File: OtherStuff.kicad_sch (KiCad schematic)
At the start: 35 parts, among them IC601 MMS9013-L-TP, IC602 MMS9013-L-TP, J601 USB_B_Micro, X601 XTAL_4_PINS, X602 XTAL_2_PINS

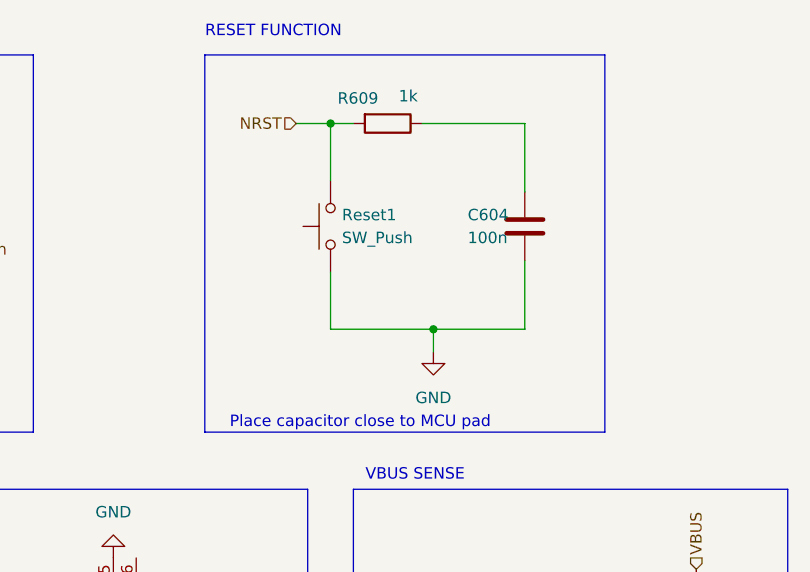
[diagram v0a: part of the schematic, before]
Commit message: Add FC0V104ZFTBR24 component library files
Added symbol, footprint, 3D model, and documentation files for the Supercap (FC0V104ZFTBR24) component across multiple EDA tool formats. Also updated schematic files and project backups, and removed obsolete autosave and backup files.
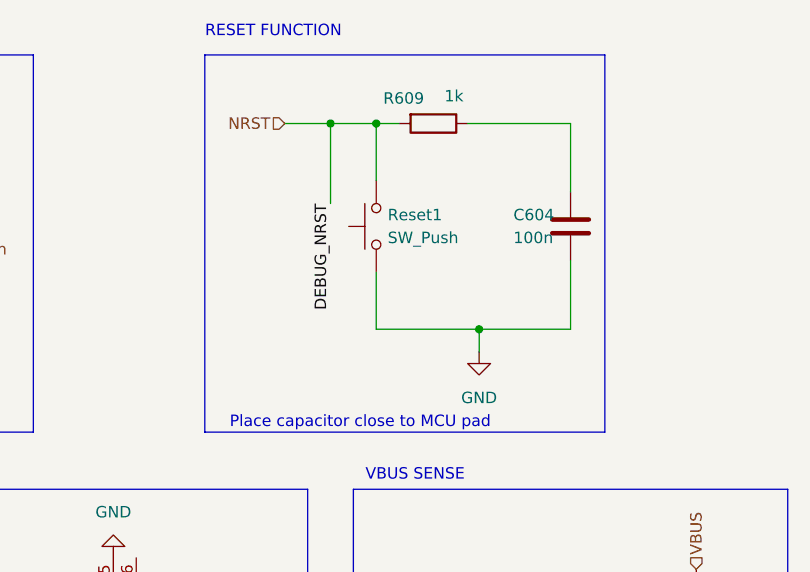
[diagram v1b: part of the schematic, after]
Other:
- moved on the sheet: C604, R609, Reset1
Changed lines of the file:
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@@
 	)
 	(junction
-		(at 97.79 29.21)
+		(at 102.87 29.21)
 		(diameter 0)
 		(color 0 0 0 0)
@@
 	)
 	(junction
+		(at 97.79 29.21)
+		(diameter 0)
+		(color 0 0 0 0)
+	)
+	(junction
 		(at 138.43 91.44)
 		(diameter 0)
@@
 	)
 	(junction
-		(at 109.22 52.07)
+		(at 114.3 52.07)
 		(diameter 0)
 		(color 0 0 0 0)
@@
 	(wire
 		(pts
-			(xy 119.38 36.83) (xy 119.38 29.21)
+			(xy 124.46 36.83) (xy 124.46 29.21)
 		)
 		(stroke
@@
 	(wire
 		(pts
-			(xy 109.22 52.07) (xy 97.79 52.07)
+			(xy 97.79 29.21) (xy 102.87 29.21)
+		)
+		(stroke
+			(width 0)
+			(type default)
+		)
+	)
+	(wire
+		(pts
+			(xy 114.3 52.07) (xy 102.87 52.07)
 		)
 		(stroke
@@
 	(wire
 		(pts
-			(xy 109.22 52.07) (xy 109.22 54.61)
+			(xy 114.3 52.07) (xy 114.3 54.61)
 		)
 		(stroke
@@
 	(wire
 		(pts
-			(xy 119.38 52.07) (xy 109.22 52.07)
+			(xy 124.46 52.07) (xy 114.3 52.07)
+		)
+		(stroke
+			(width 0)
+			(type default)
+		)
+	)
+	(wire
+		(pts
+			(xy 97.79 29.21) (xy 97.79 38.1)
 		)
 		(stroke
@@
 	(wire
 		(pts
-			(xy 97.79 52.07) (xy 97.79 45.72)
+			(xy 102.87 52.07) (xy 102.87 45.72)
 		)
 		(stroke
@@
 	(wire
 		(pts
-			(xy 97.79 29.21) (xy 100.33 29.21)
+			(xy 102.87 29.21) (xy 105.41 29.21)
 		)
 		(stroke
@@
 	(wire
 		(pts
-			(xy 93.98 29.21) (xy 97.79 29.21)
+			(xy 92.71 29.21) (xy 97.79 29.21)
 		)
 		(stroke
@@
 	(wire
 		(pts
-			(xy 119.38 29.21) (xy 107.95 29.21)
+			(xy 124.46 29.21) (xy 113.03 29.21)
 		)
 		(stroke
@@
 	(wire
 		(pts
-			(xy 119.38 44.45) (xy 119.38 52.07)
+			(xy 124.46 44.45) (xy 124.46 52.07)
 		)
 		(stroke
@@
 	(wire
 		(pts
-			(xy 97.79 35.56) (xy 97.79 29.21)
+			(xy 102.87 35.56) (xy 102.87 29.21)
 		)
 		(stroke
@@
 		)
 	)
+	(label "DEBUG_NRST"
+		(at 97.79 38.1 270)
+		(effects
+			(font
+				(size 1.27 1.27)
+			)
+			(justify right bottom)
+		)
+	)
 	(label "USB_1_D-"
 		(at 44.45 85.09 0)
@@
 	(hierarchical_label "NRST"
 		(shape input)
-		(at 93.98 29.21 180)
+		(at 92.71 29.21 180)
 		(effects
 			(font
@@
 	(symbol
 		(lib_id "Device:R")
-		(at 104.14 29.21 270)
+		(at 109.22 29.21 270)
 		(unit 1)
 		(exclude_from_sim no)
@@
 		(dnp no)
 		(property "Reference" "R609"
-			(at 100.838 26.416 90)
+			(at 105.918 26.416 90)
 			(effects
 				(font
@@
 		)
 		(property "Value" "1k"
-			(at 106.426 26.162 90)
+			(at 111.506 26.162 90)
 			(effects
 				(font
@@
 		)
 		(property "Footprint" "Resistor_SMD:R_0805_2012Metric_Pad1.20x1.40mm_HandSolder"
-			(at 104.14 27.432 90)
+			(at 109.22 27.432 90)
 			(effects
 				(font
@@
 		)
 		(property "Datasheet" "~"
-			(at 104.14 29.21 0)
+			(at 109.22 29.21 0)
 			(effects
 				(font
@@
 		)
 		(property "Description" ""
-			(at 104.14 29.21 0)
+			(at 109.22 29.21 0)
 			(effects
 				(font
@@
 		)
 		(property "Mouser Part Number" "279-CRG0805ZR"
-			(at 104.14 29.21 0)
+			(at 109.22 29.21 0)
 			(effects
 				(font
@@
 	(symbol
 		(lib_id "Device:C")
-		(at 119.38 40.64 180)
+		(at 124.46 40.64 180)
 		(unit 1)
 		(exclude_from_sim no)
@@
 		(dnp no)
 		(property "Reference" "C604"
-			(at 113.03 39.37 0)
+			(at 118.11 39.37 0)
 			(effects
 				(font
@@
 		)
 		(property "Value" "100n"
-			(at 113.03 41.91 0)
+			(at 118.11 41.91 0)
 			(effects
 				(font
@@
 		)
 		(property "Footprint" "Capacitor_SMD:C_0805_2012Metric_Pad1.18x1.45mm_HandSolder"
-			(at 118.4148 36.83 0)
+			(at 123.4948 36.83 0)
 			(effects
 				(font
@@
 		)
 		(property "Datasheet" "~"
-			(at 119.38 40.64 0)
+			(at 124.46 40.64 0)
 			(effects
 				(font
@@
 		)
 		(property "Description" ""
-			(at 119.38 40.64 0)
+			(at 124.46 40.64 0)
 			(effects
 				(font
@@
 		)
 		(property "Mouser Part Number" "187-CL21A226KQCLRNC"
-			(at 119.38 40.64 0)
+			(at 124.46 40.64 0)
 			(effects
 				(font
@@
 	(symbol
 		(lib_id "power:GND")
-		(at 109.22 54.61 0)
+		(at 114.3 54.61 0)
 		(unit 1)
 		(exclude_from_sim no)
@@
 		(fields_autoplaced yes)
 		(property "Reference" "#PWR0613"
-			(at 109.22 60.96 0)
+			(at 114.3 60.96 0)
 			(effects
 				(font
@@
 		)
 		(property "Value" "GND"
-			(at 109.22 59.69 0)
+			(at 114.3 59.69 0)
 			(effects
 				(font
@@
 		)
 		(property "Footprint" ""
-			(at 109.22 54.61 0)
+			(at 114.3 54.61 0)
 			(effects
 				(font
@@
 		)
 		(property "Datasheet" ""
-			(at 109.22 54.61 0)
+			(at 114.3 54.61 0)
 			(effects
 				(font
@@
 		)
 		(property "Description" "Power symbol creates a global label with name \"GND\" , ground"
-			(at 109.22 54.61 0)
+			(at 114.3 54.61 0)
 			(effects
 				(font
@@
 	(symbol
 		(lib_id "Switch:SW_Push")
-		(at 97.79 40.64 90)
+		(at 102.87 40.64 90)
 		(unit 1)
 		(exclude_from_sim no)
@@
 		(fields_autoplaced yes)
 		(property "Reference" "Reset1"
-			(at 99.06 39.3699 90)
+			(at 104.14 39.3699 90)
 			(effects
 				(font
@@
 		)
 		(property "Value" "SW_Push"
-			(at 99.06 41.9099 90)
+			(at 104.14 41.9099 90)
 			(effects
 				(font
@@
 		)
 		(property "Footprint" "Button_Switch_SMD:SW_Push_SPST_NO_Alps_SKRK"
-			(at 92.71 40.64 0)
+			(at 97.79 40.64 0)
 			(effects
 				(font
@@
 		)
 		(property "Datasheet" "~"
-			(at 92.71 40.64 0)
+			(at 97.79 40.64 0)
 			(effects
 				(font
@@
 		)
 		(property "Description" "Push button switch, generic, two pins"
-			(at 97.79 40.64 0)
+			(at 102.87 40.64 0)
 			(effects
 				(font

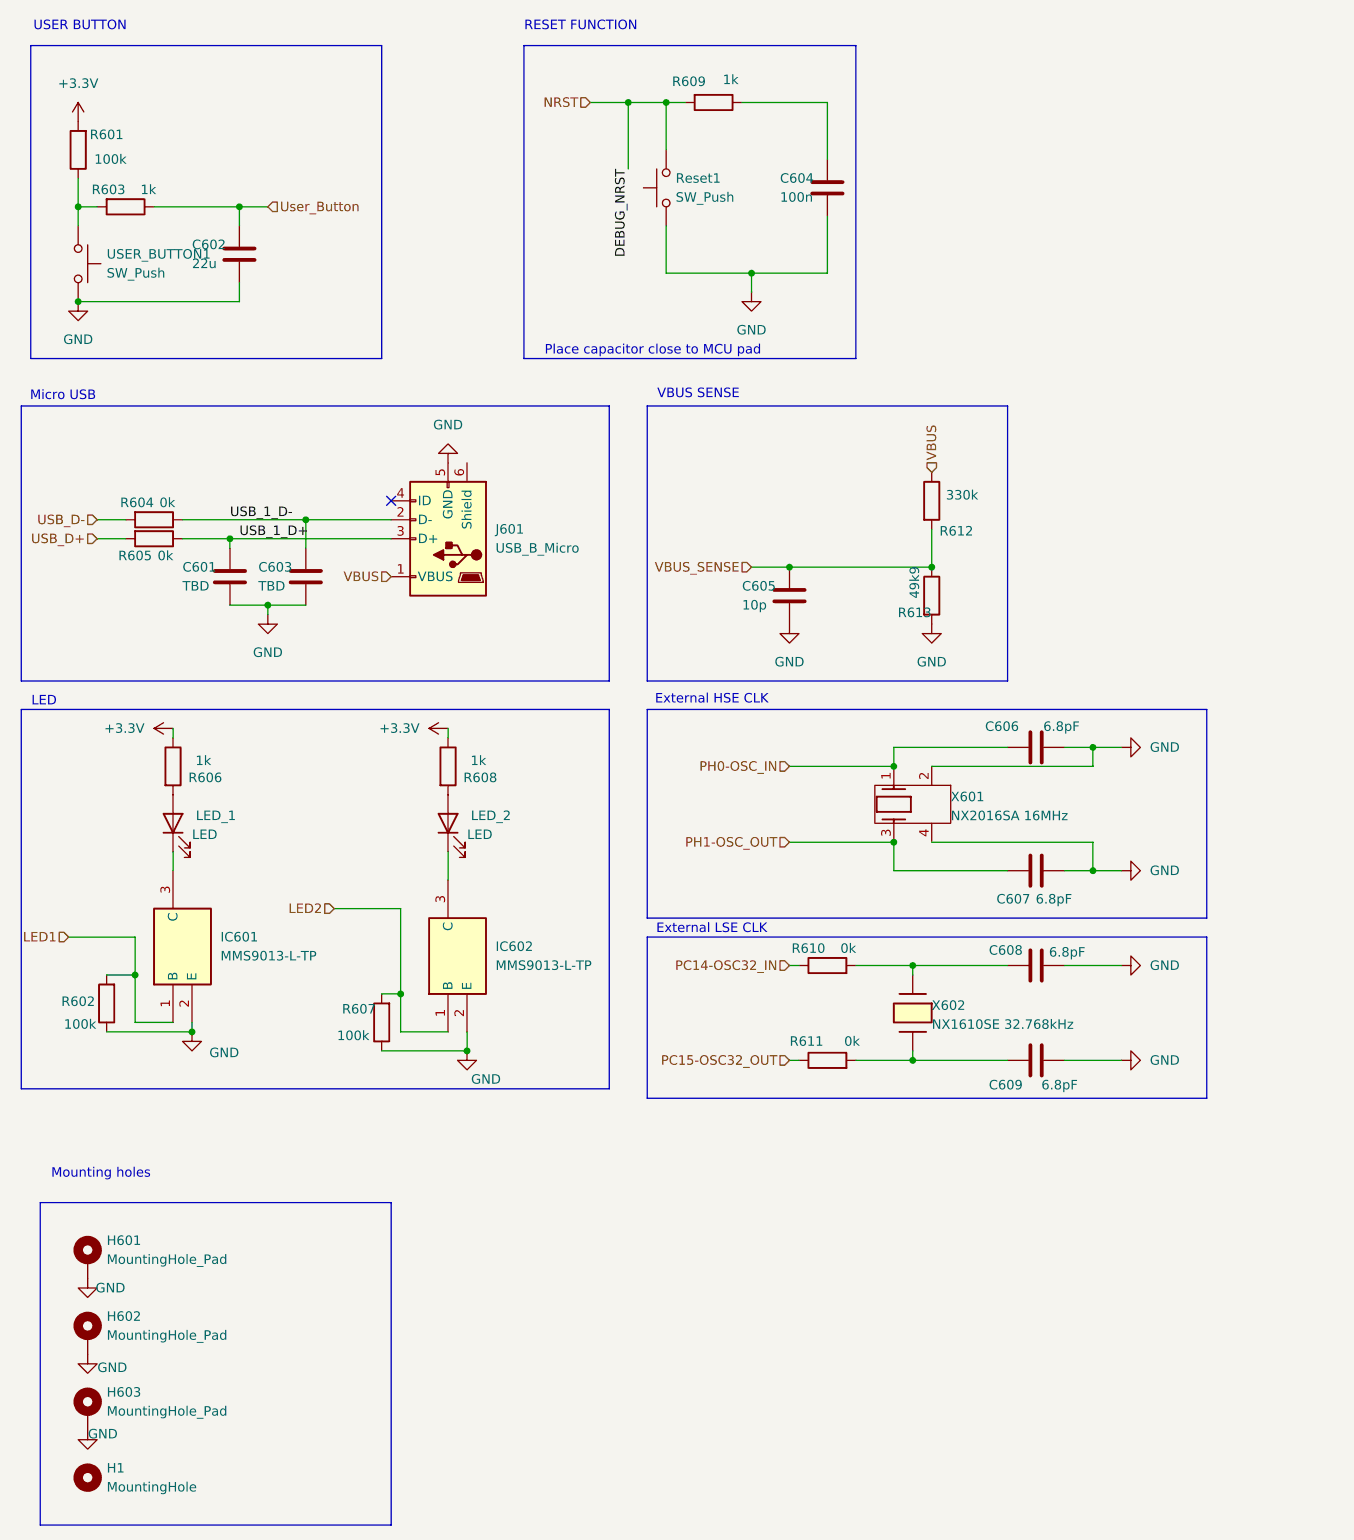
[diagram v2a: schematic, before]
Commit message: new layout
- recreation of the layout
- changed connection of ADC to MCU
- cleaner layout
- battery (supercap) for rtc
- crystal nearby the mcu
- 3V3 layer can be switched on/off separated from the mcu
- diode replaced with MOSFET
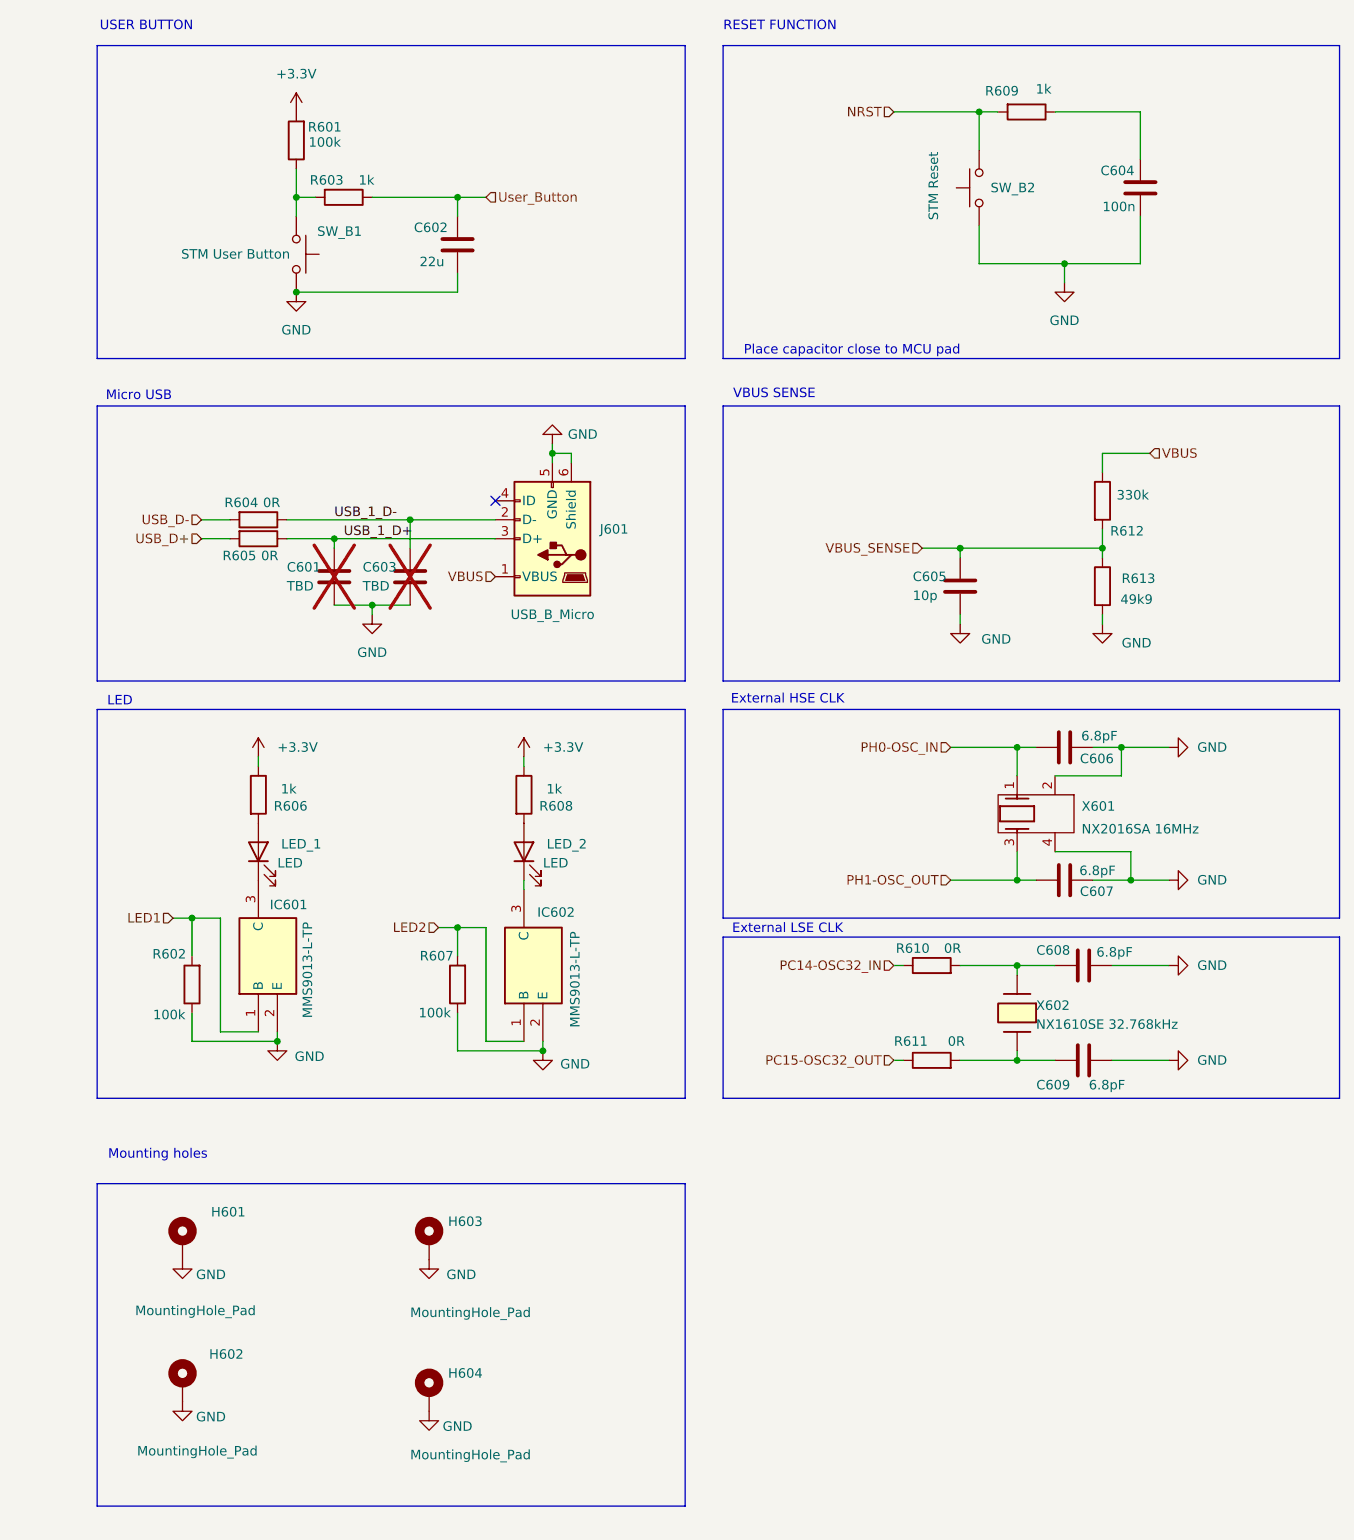
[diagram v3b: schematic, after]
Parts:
- removed H1: MountingHole, MountingHole:MountingHole_2.2mm_M2_DIN965, symbol Mechanical:MountingHole
- added H604: MountingHole_Pad, MountingHole:MountingHole_2.2mm_M2_DIN965_Pad, symbol Mechanical:MountingHole_Pad
- C601, C603: Mouser Part Number 187-CL21A226KQCLRNC -> (none); now not fitted
- C604: Mouser Part Number 187-CL21A226KQCLRNC -> 603-CC805KRX7R9BB104
- C605: Mouser Part Number 187-CL21A226KQCLRNC -> 80-C0805C100JCRACTU
- C606, C607, C608, C609: Mouser Part Number 187-CL21A226KQCLRNC -> 581-08055A6R8D
- J601: Mouser Part Number (none) -> 649-10103594-0001LF
- LED_1, LED_2: Mouser Part Number (none) -> 630-HSME-C170
- R601, R602, R607: Mouser Part Number 279-CRG0805ZR -> 660-RK73B2ATTE104J
- R603, R606, R608, R609: Mouser Part Number 279-CRG0805ZR -> 667-ERJ-6ENF1001V
- R604, R605, R610, R611: value 0k -> 0R
- R612: Mouser Part Number 279-CRG0805ZR -> 652-CR0805AFX3303EAS
- R613: Mouser Part Number 279-CRG0805ZR -> 594-MCU08050D4992BP5
- SW_B1: renamed from USER_BUTTON1; Mouser Part Number (none) -> 688-SKRKAG
- SW_B2: renamed from Reset1; Mouser Part Number (none) -> 688-SKRKAG
- X601: Mouser Part Number (none) -> 344-NX1610SA32768000; Mouser Price/Stock (none) -> MU00658-32.768K (Digikey)
- X602: footprint NX1610SE:NX1610SE -> Bibliothek:NX1610SA32768000kHz
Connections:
- net GND: now also J601.6 (Shield), H604.1
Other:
- moved on the sheet: C602, C604, C605, C606, C607, C608, C609, H601, H602, H603, IC601, IC602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
